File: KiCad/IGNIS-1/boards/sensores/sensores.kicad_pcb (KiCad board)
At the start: 2 copper layers, 62 x 62 mm, 16 parts, among them J41 Backplane_2x10, U20 BME280, U21 MPU6050, U22 MQ-135, U24 GPS NEO-6M, U3 Boost_5V

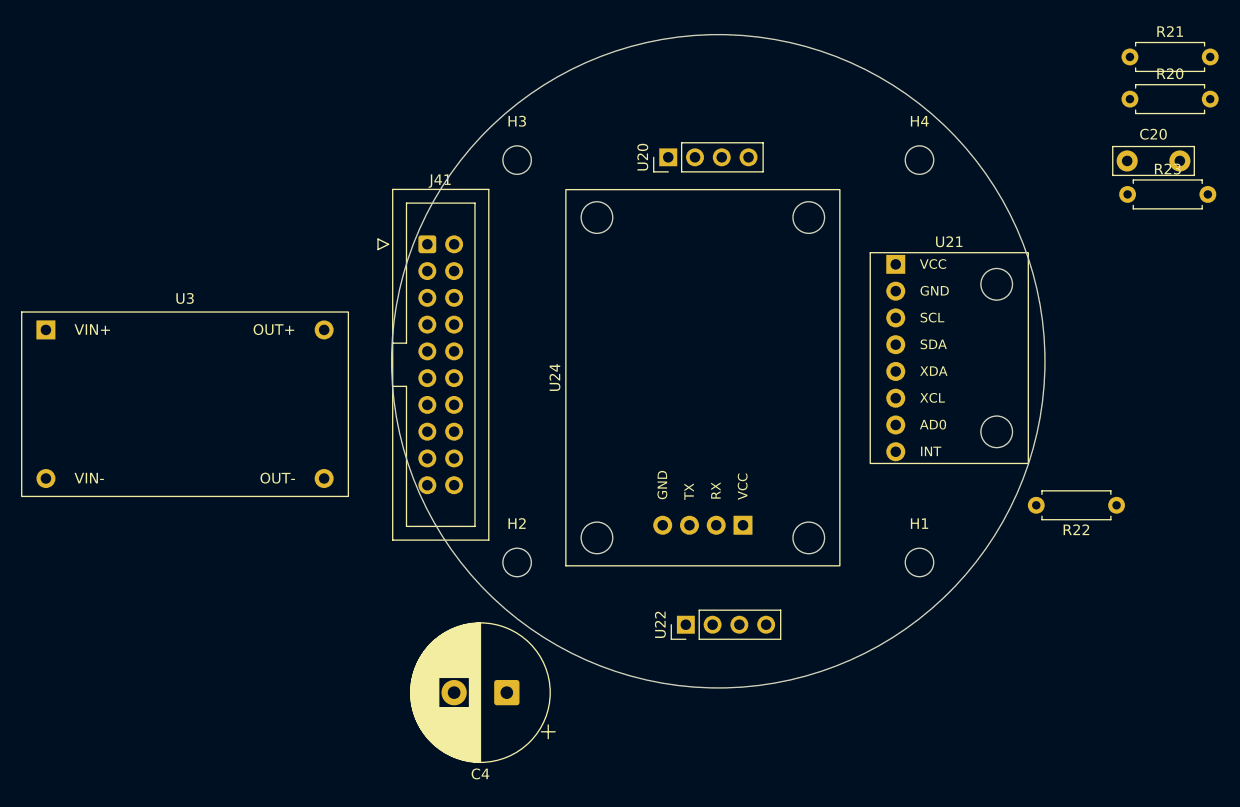
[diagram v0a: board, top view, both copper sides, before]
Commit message: Energia: split en 2 boards (carga + energia) y redistribucion de rieles
- Board carga (5º): TP4056 + bateria + RBF + SW1 + TPS63020 -> +3V3 y VSW al bus
- Board energia (4º): MT3608 -> +5V al bus (toma VSW)
- Simbolos nuevos: TP4056, TPS63020; footprints TP4056_HW373, SW_Slide_SS12D00
- Bus: +3V3(p1), +5V(p19), VSW(p20), GND(2/4/11); backplane a header plano
- cerebro: quitada seccion de energia duplicada (U2/J1/J2/SW1/C1), +3V3 del bus
- sensores: quitado MT3608 (U3), +5V del bus alimenta MQ-135/GPS
- ZC323200 eliminado (sin uso)

Co-Authored-By: Claude Opus 4.8 <noreply@anthropic.com>
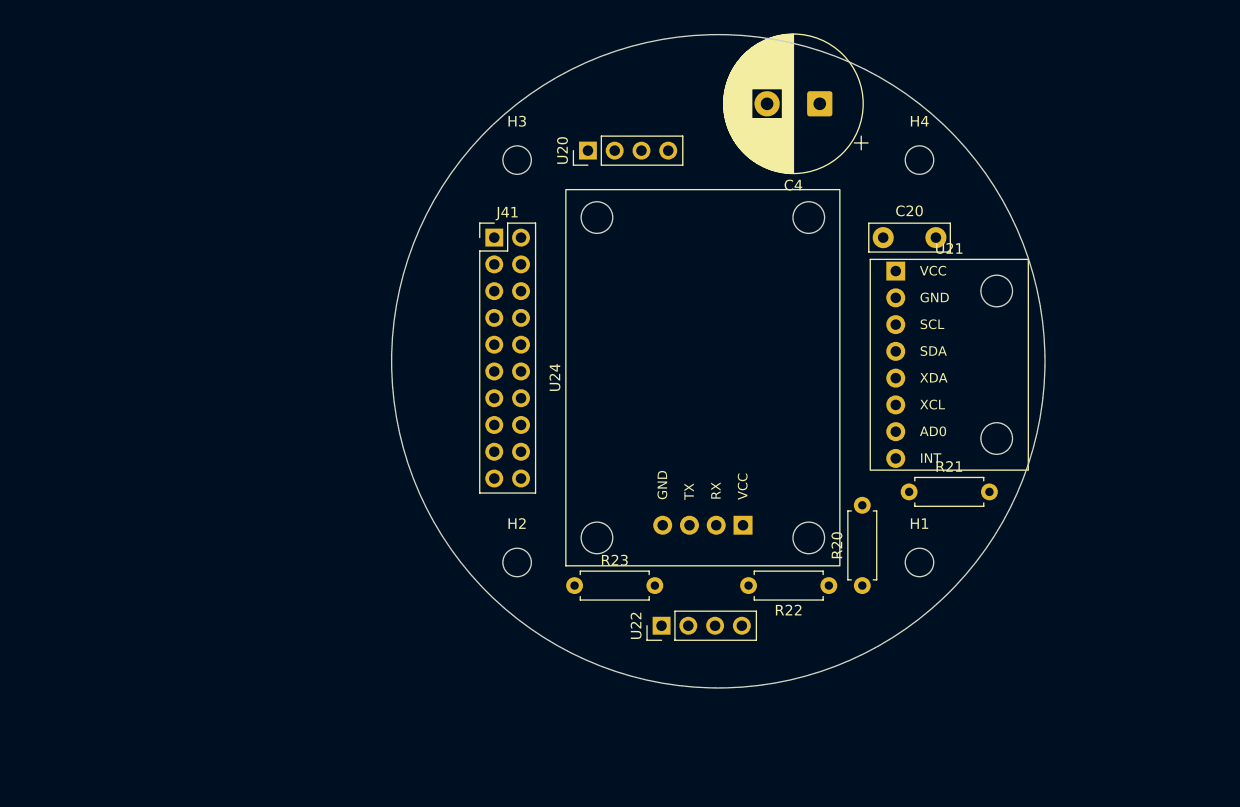
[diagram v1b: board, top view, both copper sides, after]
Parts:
- removed U3: Boost_5V, IGNIS1:MT3608_module
- J41: footprint Connector_IDC:IDC-Header_2x10_P2.54mm_Vertical -> Connector_PinHeader_2.54mm:PinHeader_2x10_P2.54mm_Vertical
- moved R23 64.3 mm to (86.4, 121.3)
- moved C4 63.3 mm to (109.6, 75.6)
- moved R20 52.7 mm to (113.7, 121.3), turned to 90 degrees
- moved R21 46.3 mm to (118.1, 112.4)
- moved R22 28.3 mm to (110.5, 121.3)
- moved C20 24.3 mm to (115.7, 88.3)
- moved U20 7.65 mm to (87.6, 80.0)
- moved J41 6.38 mm to (78.7, 88.3)
- moved U22 2.31 mm to (94.6, 125.1)
- moved U21 0.64 mm to (121.9, 100.3)
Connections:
- J41 pad 19: unconnected-(J41-Pin_19-Pad19) -> +5V
